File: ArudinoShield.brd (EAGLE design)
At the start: 53.3 x 59.4 mm, 25 parts, among them IC1 L298, U1 REG1117

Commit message: minor changes
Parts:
- moved D6 5.08 mm to (80.0, 22.9)
- moved OUT2 2.54 mm to (66.0, 24.1)
- moved OUT1 2.54 mm to (55.9, 24.1)
- moved VIN 2.54 mm to (45.7, 24.1)
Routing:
- net +5V: track 91.9 -> 94.7 mm
- net VIN: track 128.2 -> 126.0 mm
- net OUT2: track 33.0 -> 35.1 mm
- net OUT1: track 23.5 -> 24.5 mm
- net N$11: track 23.3 -> 22.6 mm
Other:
- board text added: "Designed by: Adam Fuller"

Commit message: updated schematic and board to use DC jack
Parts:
- VIN: device con-amp:1X2MTA -> con-jack:SPC4078
- moved VIN 1.27 mm to (45.7, 25.4), turned to 90 degrees
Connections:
- net GND: now also VIN.3; no longer VIN.2
- net VIN: now also VIN.2
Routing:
- net VIN: track 126.0 -> 136.7 mm
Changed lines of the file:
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@@
 <drawing>
 <settings>
-<setting alwaysvectorfont="yes"/>
+<setting alwaysvectorfont="no"/>
 <setting verticaltext="up"/>
 </settings>
@@
 <attribute name="VALUE" x="69.596" y="46.228" size="1.27" layer="27" ratio="10"/>
 </element>
-<element name="VIN" library="con-amp" library_urn="urn:adsk.eagle:library:127" package="1X2MTA" package3d_urn="urn:adsk.eagle:package:8081562/1" value="" x="45.72" y="24.13" smashed="yes">
-<attribute name="NAME" x="38.8112" y="24.13" size="1.778" layer="25" rot="R270"/>
-<attribute name="POPULARITY" value="4" x="45.72" y="24.13" size="1.778" layer="27" display="off"/>
-<attribute name="VALUE" x="42.2831" y="28.5448" size="1.27" layer="27"/>
-</element>
 <element name="OUT3" library="con-amp" library_urn="urn:adsk.eagle:library:127" package="1X2MTA" package3d_urn="urn:adsk.eagle:package:8081562/1" value="" x="71.12" y="72.39" smashed="yes" rot="R180">
 <attribute name="NAME" x="78.0288" y="66.04" size="1.778" layer="25" rot="R90"/>
@@
 <attribute name="SPICEPREFIX" value="R" x="49.53" y="74.93" size="1.778" layer="27" display="off"/>
 <attribute name="VALUE" x="47.2694" y="74.295" size="1.27" layer="27" ratio="10"/>
+</element>
+<element name="VIN" library="con-jack" library_urn="urn:adsk.eagle:library:154" package="SPC4078" package3d_urn="urn:adsk.eagle:package:7494/1" value="" x="45.72" y="25.4" smashed="yes" rot="R90">
+<attribute name="MF" value="" x="45.72" y="25.4" size="1.778" layer="27" rot="R90" display="off"/>
+<attribute name="MPN" value="" x="45.72" y="25.4" size="1.778" layer="27" rot="R90" display="off"/>
+<attribute name="NAME" x="40.64" y="15.24" size="1.27" layer="25" rot="R90"/>
+<attribute name="OC_FARNELL" value="unknown" x="45.72" y="25.4" size="1.778" layer="27" rot="R90" display="off"/>
+<attribute name="OC_NEWARK" value="unknown" x="45.72" y="25.4" size="1.778" layer="27" rot="R90" display="off"/>
+<attribute name="POPULARITY" value="3" x="45.72" y="25.4" size="1.778" layer="27" rot="R90" display="off"/>
+<attribute name="VALUE" x="52.07" y="15.24" size="1.27" layer="27" rot="R90"/>
 </element>
 </elements>
@@
 <contactref element="HC05" pad="3"/>
 <contactref element="R2" pad="1"/>
-<contactref element="VIN" pad="2"/>
 <polygon width="0.4064" layer="16">
 <vertex x="35.56" y="78.74"/>
@@
 <wire x1="66.0239" y1="44.8149" x2="70.1294" y2="48.9204" width="1.143" layer="1"/>
 <wire x1="66.0239" y1="41.91" x2="66.0239" y2="44.8149" width="1.143" layer="1"/>
+<contactref element="VIN" pad="3"/>
 </signal>
 <signal name="VIN">
@@
 <contactref element="U1" pad="3"/>
 <contactref element="IC1" pad="4"/>
-<contactref element="VIN" pad="1"/>
-<wire x1="43.18" y1="33.02" x2="46.99" y2="29.21" width="1.143" layer="1"/>
-<wire x1="46.99" y1="29.21" x2="46.99" y2="24.13" width="1.143" layer="1"/>
-<wire x1="47.7012" y1="24.13" x2="46.99" y2="24.13" width="1.143" layer="1"/>
+<wire x1="43.18" y1="33.02" x2="40.64" y2="30.48" width="1.143" layer="1"/>
+<wire x1="40.64" y1="30.48" x2="40.64" y2="24.13" width="1.143" layer="1"/>
 <wire x1="43.18" y1="38.1" x2="43.18" y2="33.02" width="1.143" layer="1"/>
 <wire x1="44.45" y1="45.72" x2="58.42" y2="45.72" width="1.143" layer="1"/>
@@
 <wire x1="43.18" y1="44.45" x2="43.18" y2="38.1" width="1.143" layer="1"/>
 <wire x1="80.01" y1="62.23" x2="77.47" y2="62.23" width="1.143" layer="1"/>
-<wire x1="82.55" y1="20.6375" x2="51.1937" y2="20.6375" width="1.143" layer="1"/>
-<wire x1="47.7012" y1="24.13" x2="51.1937" y2="20.6375" width="1.143" layer="1"/>
+<wire x1="51.1937" y1="20.6375" x2="82.55" y2="20.6375" width="1.143" layer="1"/>
 <wire x1="75.3618" y1="48.26" x2="74.7014" y2="48.9204" width="1.143" layer="1"/>
 <wire x1="82.55" y1="26.67" x2="82.55" y2="20.6375" width="1.143" layer="1"/>
@@
 <wire x1="80.01" y1="48.26" x2="78.74" y2="48.26" width="1.143" layer="1"/>
 <wire x1="78.74" y1="48.26" x2="75.3618" y2="48.26" width="1.143" layer="1"/>
+<contactref element="VIN" pad="2"/>
+<contactref element="VIN" pad="1"/>
+<wire x1="45.72" y1="22.4" x2="42.37" y2="22.4" width="1.143" layer="1"/>
+<wire x1="42.37" y1="22.4" x2="40.64" y2="24.13" width="1.143" layer="1"/>
+<wire x1="45.72" y1="22.4" x2="48.72" y2="25.4" width="1.143" layer="1"/>
+<wire x1="48.72" y1="25.4" x2="50.52" y2="25.4" width="1.143" layer="1"/>
+<wire x1="50.52" y1="25.4" x2="51.1937" y2="24.7263" width="1.143" layer="1"/>
+<wire x1="51.1937" y1="24.7263" x2="51.1937" y2="20.6375" width="1.143" layer="1"/>
 </signal>
 <signal name="9GPWM">

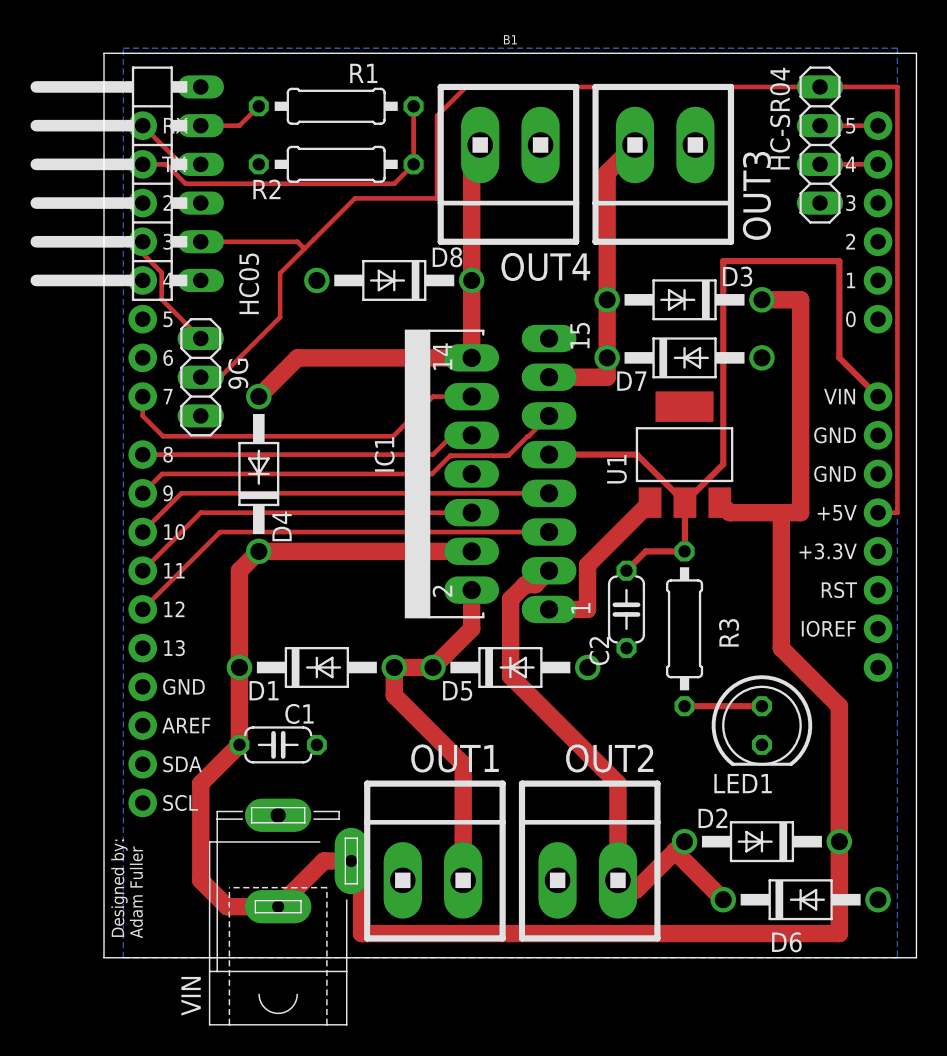
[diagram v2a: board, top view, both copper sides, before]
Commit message: shifted L298 to make room for heat sink
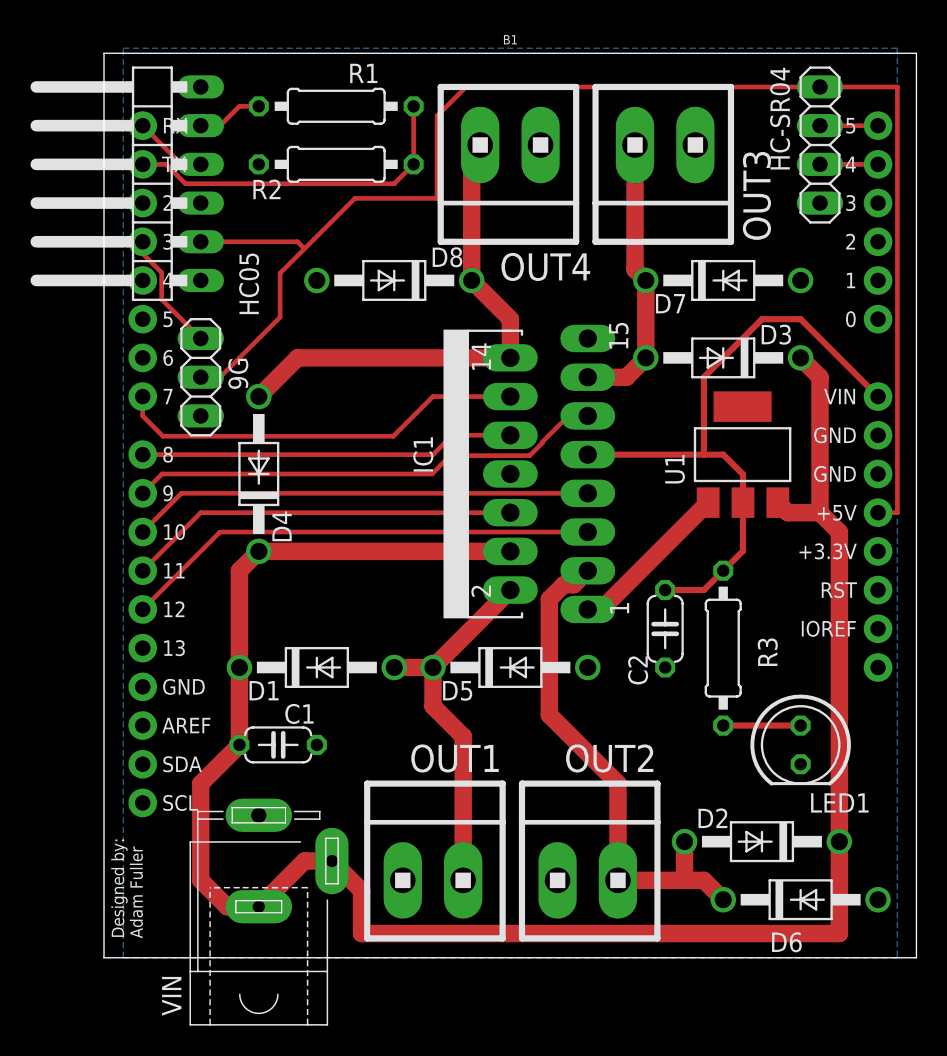
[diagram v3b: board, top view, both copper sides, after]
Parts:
- moved D7 5.68 mm to (74.9, 63.5)
- moved D3 4.58 mm to (74.9, 58.4)
- moved U1 3.81 mm to (76.2, 52.1)
- moved R3 2.84 mm to (74.9, 39.4)
- moved C2 2.84 mm to (71.1, 40.6)
- moved LED1 2.84 mm to (80.0, 33.0)
- moved IC1 2.54 mm to (58.4, 50.8)
- moved VIN 1.27 mm to (44.5, 25.4)
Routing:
- net +5VIN: track 52.2 -> 42.1 mm
- net VIN: track 136.7 -> 129.0 mm
- net OUT4: track 29.2 -> 32.8 mm
- net ENB: track 28.8 -> 31.4 mm
- net IN2: track 27.7 -> 30.3 mm
- net IN1: track 28.8 -> 31.3 mm
- net IN4: track 24.5 -> 27.0 mm
- net IN3: track 22.1 -> 24.7 mm
- net ENA: track 23.2 -> 25.7 mm
- net OUT2: track 35.1 -> 33.6 mm
- net OUT3: track 19.8 -> 18.6 mm
